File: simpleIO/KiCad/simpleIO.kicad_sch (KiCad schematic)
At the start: 48 parts, among them J1 Conn_02x17_Odd_Even

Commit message: Changing audio connector
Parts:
- AUDIO1: footprint Connector_Audio:Jack_3.5mm_PJ311_Horizontal -> audio-jack:CUI_SJ-43516-SMT
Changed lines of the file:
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@@
 			)
 		)
-		(property "Footprint" "Connector_Audio:Jack_3.5mm_PJ311_Horizontal"
+		(property "Footprint" "audio-jack:CUI_SJ-43516-SMT"
 			(at 107.95 114.3 0)
 			(effects

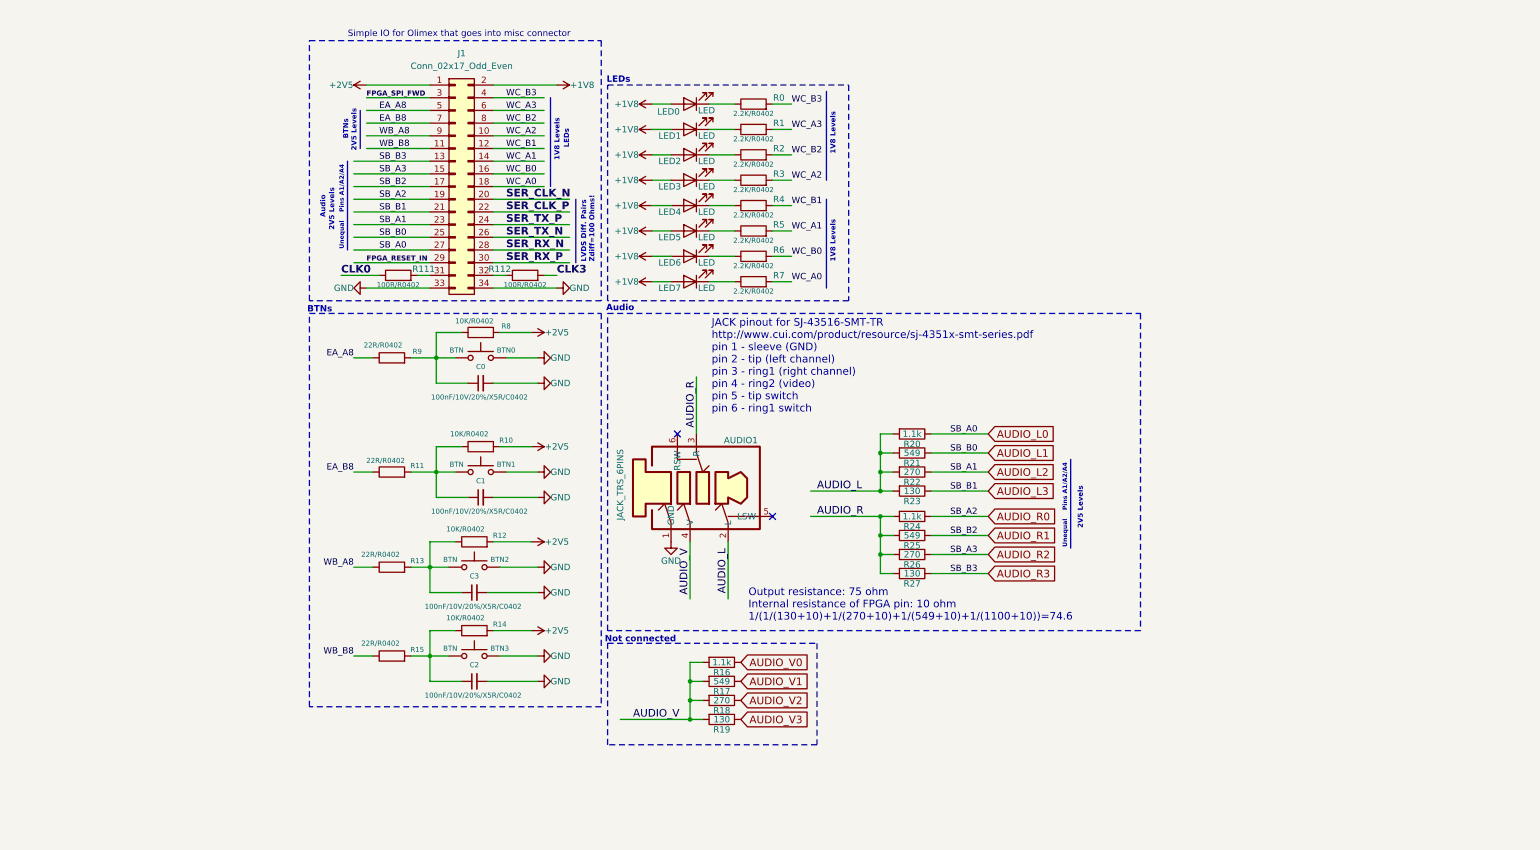
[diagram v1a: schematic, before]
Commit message: Moving schematics to v9 adding more details
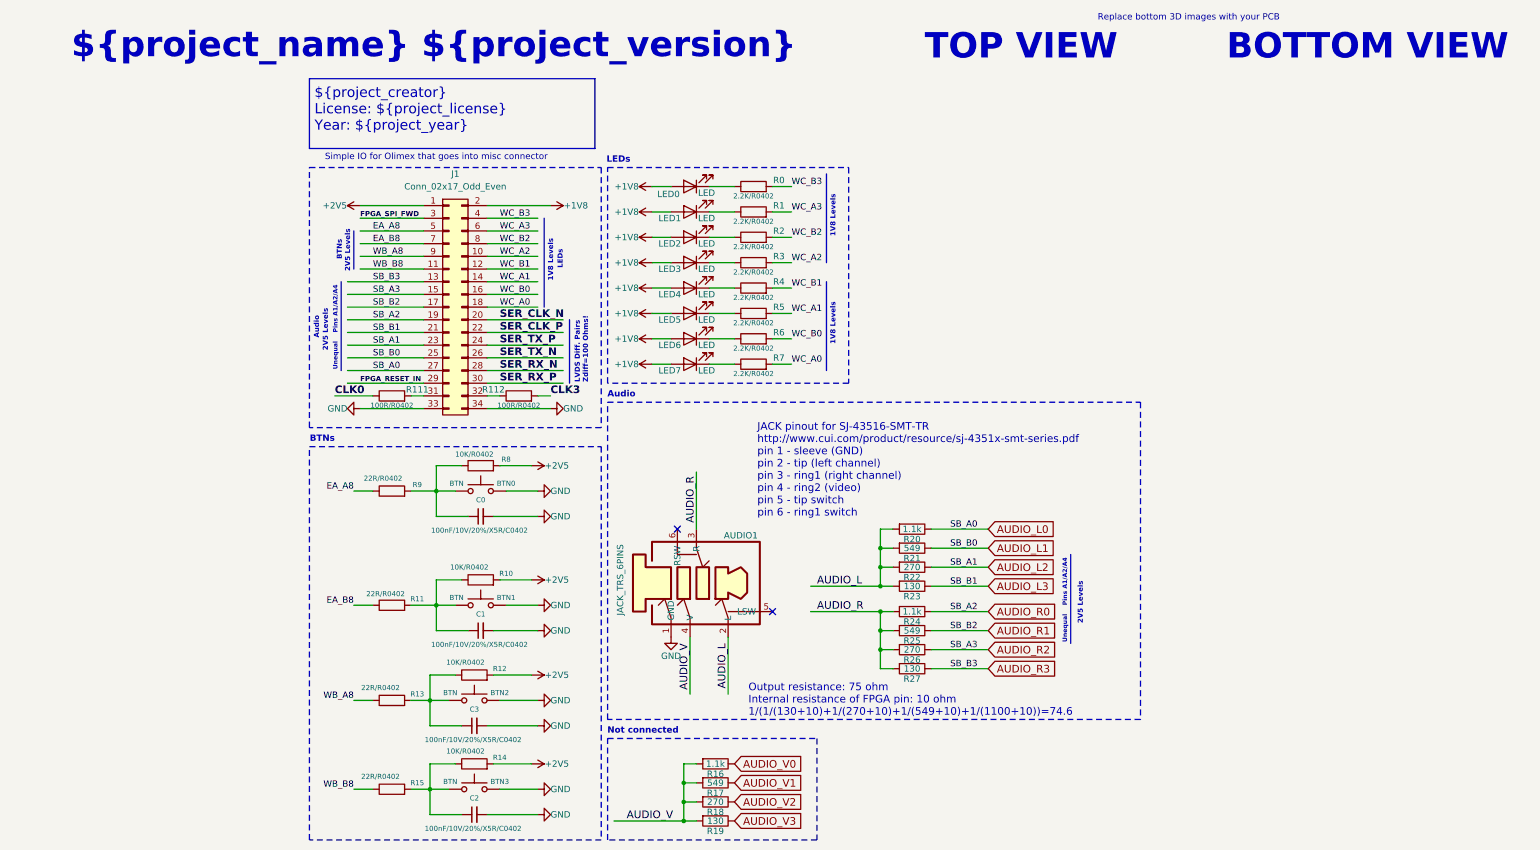
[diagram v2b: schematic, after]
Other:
- note added: "${project_creator} License: ${project_license} Year: ${project_year}"
- note added: "${project_name} ${project_version}"
- note added: "BOTTOM VIEW"
- note added: "Replace bottom 3D images with your PCB"
- note added: "TOP VIEW"
- company: (none) -> ${project_creator}
- title: (none) -> ${project_name} ${project_version}
- moved on the sheet: AUDIO1, BTN0, BTN1, BTN2, BTN3, C0, C1, C2, C3, J1, LED0, LED1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
